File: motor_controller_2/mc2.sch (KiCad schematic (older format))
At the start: 56 parts, among them P1 Battery, P2 Servo, P3 Uart, P4 Ultrasound, P5 Motor left, P6 Motor right, P7 ISP, U1 TS1117E33, U2 TS1117E50, U3 PC817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

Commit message: footprints assigned (not ready)
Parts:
- added P8: RPi 5V, Pin_Headers:Pin_Header_Straight_1x02, symbol CONN_01X02
- C10, C11, C12, C60, C61, C62, C63, C80, C81, C91: footprint (none) -> Capacitors_SMD:C_0603_HandSoldering
- C13, C14, C20, C21: footprint (none) -> SMD_Packages:SMD-1206_Pol
- C90: renamed from C91; footprint (none) -> Capacitors_SMD:C_0603_HandSoldering
- D10: footprint (none) -> Diodes_SMD:DO-214AB_Handsoldering
- D11, D60, D61, R11, R12, R13, R30, R31, R40, R41, R60, R61, R62, R70, R71, R72, R73, R74, R75, R76, R77: footprint (none) -> Resistors_SMD:R_0603_HandSoldering
- P1, P5, P6: footprint (none) -> Pin_Headers:Pin_Header_Straight_1x02
- P2, P3: footprint (none) -> Pin_Headers:Pin_Header_Straight_1x03
- P4: footprint (none) -> Pin_Headers:Pin_Header_Straight_1x04
- P7: footprint (none) -> Pin_Headers:Pin_Header_Straight_2x03
- R100: renamed from R70; footprint (none) -> Resistors_SMD:R_0603_HandSoldering
- R101: renamed from R71; footprint (none) -> Resistors_SMD:R_0603_HandSoldering
- U3, U4: footprint DIP-4 -> (none)
- U6: footprint TQFP44 -> Housings_QFP:TQFP-44_10x10mm_Pitch0.8mm
- renumbered U7 to U10
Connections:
- net +5VD: now also P8.2 (P2)
- net GND: now also P8.1 (P1)

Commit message: footprint assignments (not ready)
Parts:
- U1, U2: footprint (none) -> kicad-libraries:SOT-223
- U10: footprint (none) -> TO_SOT_Packages_SMD:SOT-23-5
- U5: footprint (none) -> Pin_Headers:Pin_Header_Angled_1x03
- U7: footprint (none) -> kicad-libraries:SOIC16
- U8, U9: footprint (none) -> kicad-libraries:SOP8
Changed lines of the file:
@@
 F 0 "U1" H 4500 600 50  0000 C CNN
 F 1 "TS1117E33" H 4400 1100 50  0000 C CNN
-F 2 "" H 4400 850 50  0001 C CNN
+F 2 "kicad-libraries:SOT-223" H 4400 850 50  0001 C CNN
 F 3 "" H 4400 850 50  0000 C CNN
 	1    4400 850
@@
 F 0 "U2" H 4500 1950 50  0000 C CNN
 F 1 "TS1117E50" H 4400 2450 50  0000 C CNN
-F 2 "" H 4400 2200 50  0001 C CNN
+F 2 "kicad-libraries:SOT-223" H 4400 2200 50  0001 C CNN
 F 3 "" H 4400 2200 50  0000 C CNN
 	1    4400 2200
@@
 F 0 "U5" H 6750 704 50  0000 C CNN
 F 1 "R-78Bxx" H 6600 1100 50  0000 C CNN
-F 2 "" H 6600 900 50  0001 C CNN
+F 2 "Pin_Headers:Pin_Header_Angled_1x03" H 6600 900 50  0001 C CNN
 F 3 "" H 6600 900 50  0000 C CNN
 	1    6600 900
@@
 F 0 "U10" H 7800 4400 60  0000 C CNN
 F 1 "ts321" H 7850 3950 60  0000 C CNN
-F 2 "" H 7550 4450 60  0001 C CNN
+F 2 "TO_SOT_Packages_SMD:SOT-23-5" H 7550 4450 60  0001 C CNN
 F 3 "" H 7550 4450 60  0000 C CNN
 	1    7450 4200
@@
 F 0 "U8" H 9450 5150 60  0000 C CNN
 F 1 "BD6221F-E2" H 9650 4550 60  0000 C CNN
-F 2 "" H 10000 4700 60  0001 C CNN
+F 2 "kicad-libraries:SOP8" H 10000 4700 60  0001 C CNN
 F 3 "" H 10000 4700 60  0000 C CNN
 	1    9650 4850
@@
 F 0 "U7" H 1700 6200 50  0000 L CNN
 F 1 "TLP280" H 1700 5800 50  0000 L CNN
-F 2 "" H 1700 5800 50  0001 L CIN
+F 2 "kicad-libraries:SOIC16" H 1700 5800 50  0001 L CIN
 F 3 "" H 1900 6000 50  0000 L CNN
 	1    1900 6000
@@
 F 0 "U7" H 1700 7400 50  0000 L CNN
 F 1 "TLP280" H 1700 7000 50  0000 L CNN
-F 2 "" H 1700 7000 50  0001 L CIN
+F 2 "kicad-libraries:SOIC16" H 1700 7000 50  0001 L CIN
 F 3 "" H 1900 7200 50  0000 L CNN
 	2    1900 7200
@@
 F 0 "U7" H 4450 6200 50  0000 L CNN
 F 1 "TLP280" H 4450 5800 50  0000 L CNN
-F 2 "" H 4450 5800 50  0001 L CIN
+F 2 "kicad-libraries:SOIC16" H 4450 5800 50  0001 L CIN
 F 3 "" H 4650 6000 50  0000 L CNN
 	3    4650 6000
@@
 F 0 "U7" H 4450 7400 50  0000 L CNN
 F 1 "TLP280" H 4450 7000 50  0000 L CNN
-F 2 "" H 4450 7000 50  0001 L CIN
+F 2 "kicad-libraries:SOIC16" H 4450 7000 50  0001 L CIN
 F 3 "" H 4650 7200 50  0000 L CNN
 	4    4650 7200
@@
 F 0 "U9" H 9450 6050 60  0000 C CNN
 F 1 "BD6221F-E2" H 9650 5450 60  0000 C CNN
-F 2 "" H 10000 5600 60  0001 C CNN
+F 2 "kicad-libraries:SOP8" H 10000 5600 60  0001 C CNN
 F 3 "" H 10000 5600 60  0000 C CNN
 	1    9650 5750

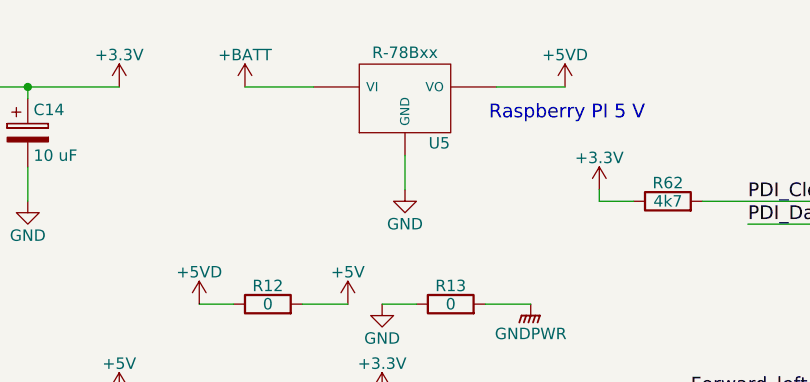
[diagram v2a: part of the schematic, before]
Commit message: all footprints assigned
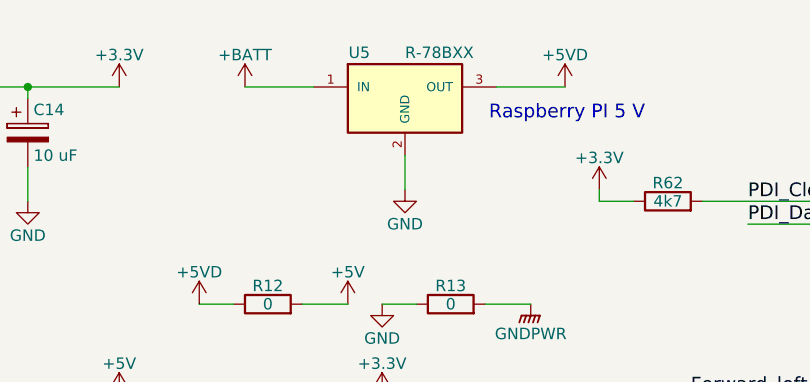
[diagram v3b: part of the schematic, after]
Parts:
- removed U5: R-78Bxx, Pin_Headers:Pin_Header_Angled_1x03, symbol 7805
- added U5: R-78BXX, TO_SOT_Packages_THT:TO-220_Neutral123_Vertical, symbol LM7806CT
- U3, U4: footprint (none) -> rzfp:OPB606
- U8, U9: footprint kicad-libraries:SOP8 -> Housings_SOIC:SOIC-8_3.9x4.9mm_Pitch1.27mm
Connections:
- net +5VD: now also U5.3 (OUT)
- net +BATT: now also U5.1 (IN)
- net GND: now also U5.2 (GND)
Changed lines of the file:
@@
 F 0 "U3" H 4100 3900 50  0000 L CNN
 F 1 "PC817" H 4300 3900 50  0000 L CNN
-F 2 "" H 4100 3500 50  0001 L CIN
+F 2 "rzfp:OPB606" H 4100 3500 50  0001 L CIN
 F 3 "" H 4300 3700 50  0000 L CNN
 	1    4300 3700
@@
 F 0 "U4" H 4100 5200 50  0000 L CNN
 F 1 "PC817" H 4300 5200 50  0000 L CNN
-F 2 "" H 4100 4800 50  0001 L CIN
+F 2 "rzfp:OPB606" H 4100 4800 50  0001 L CIN
 F 3 "" H 4300 5000 50  0000 L CNN
 	1    4300 5000
@@
 Text Label 5300 4900 2    60   ~ 0
 Rpm_left
-$Comp
-L 7805 U5
-U 1 1 57C32956
-P 6600 900
-F 0 "U5" H 6750 704 50  0000 C CNN
-F 1 "R-78Bxx" H 6600 1100 50  0000 C CNN
-F 2 "Pin_Headers:Pin_Header_Angled_1x03" H 6600 900 50  0001 C CNN
-F 3 "" H 6600 900 50  0000 C CNN
-	1    6600 900
-	1    0    0    -1
-$EndComp
 $Comp
 L +BATT #PWR026
@@
 F 0 "U8" H 9450 5150 60  0000 C CNN
 F 1 "BD6221F-E2" H 9650 4550 60  0000 C CNN
-F 2 "kicad-libraries:SOP8" H 10000 4700 60  0001 C CNN
+F 2 "Housings_SOIC:SOIC-8_3.9x4.9mm_Pitch1.27mm" H 10000 4700 60  0001 C CNN
 F 3 "" H 10000 4700 60  0000 C CNN
 	1    9650 4850
@@
 F 0 "U9" H 9450 6050 60  0000 C CNN
 F 1 "BD6221F-E2" H 9650 5450 60  0000 C CNN
-F 2 "kicad-libraries:SOP8" H 10000 5600 60  0001 C CNN
+F 2 "Housings_SOIC:SOIC-8_3.9x4.9mm_Pitch1.27mm" H 10000 5600 60  0001 C CNN
 F 3 "" H 10000 5600 60  0000 C CNN
 	1    9650 5750
@@
 	-1   0    0    1
 $EndComp
+$Comp
+L LM7806CT U5
+U 1 1 57CAF2D1
+P 6600 900
+F 0 "U5" H 6400 1100 50  0000 C CNN
+F 1 "R-78BXX" H 6600 1100 50  0000 L CNN
+F 2 "TO_SOT_Packages_THT:TO-220_Neutral123_Vertical" H 6600 1000 50  0001 C CIN
+F 3 "" H 6600 900 50  0000 C CNN
+	1    6600 900
+	1    0    0    -1
+$EndComp
 $EndSCHEMATC

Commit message: footprints finalized
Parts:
- D10: footprint Diodes_SMD:DO-214AB_Handsoldering -> Diodes_SMD:DO-214BA
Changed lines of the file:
@@
 F 0 "D10" H 1500 950 50  0000 C CNN
 F 1 "SS24" H 1500 750 50  0000 C CNN
-F 2 "Diodes_SMD:DO-214AB_Handsoldering" H 1500 850 50  0001 C CNN
+F 2 "Diodes_SMD:DO-214BA" H 1500 850 50  0001 C CNN
 F 3 "" H 1500 850 50  0000 C CNN
 	1    1500 850

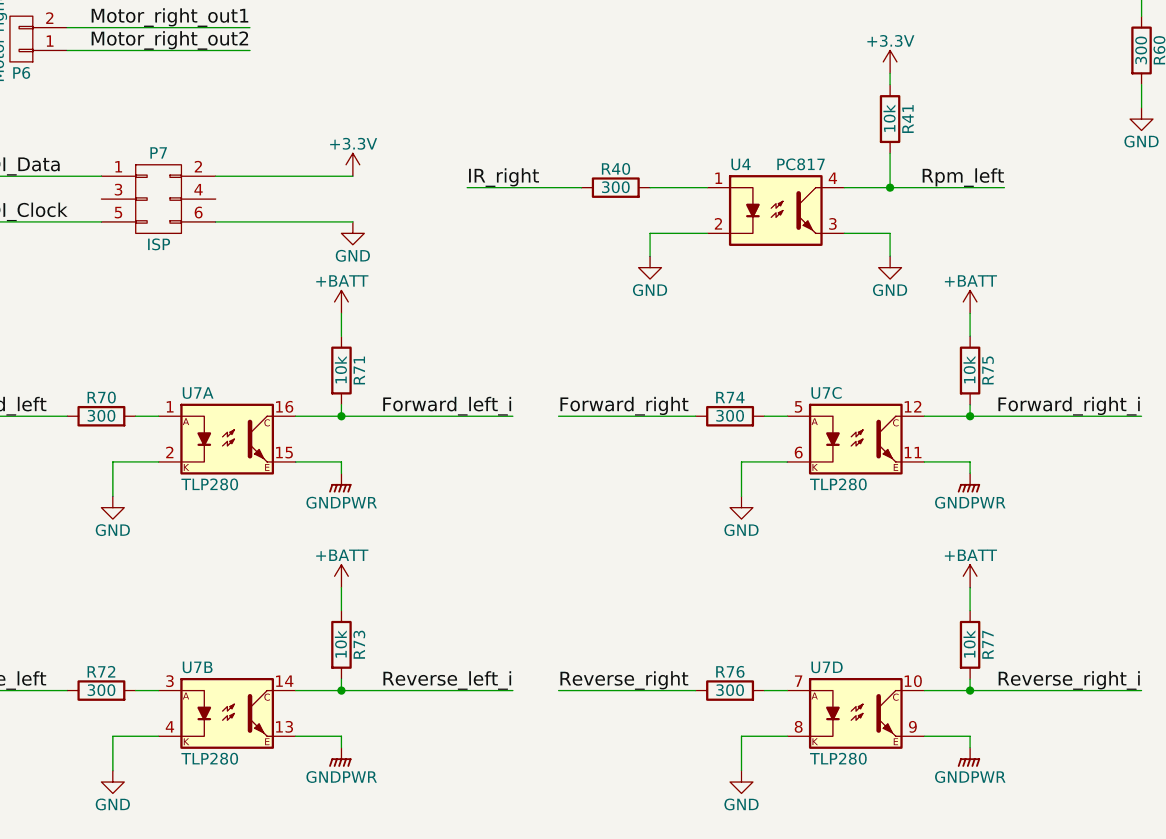
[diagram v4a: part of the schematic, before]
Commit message: component layout of motor controller
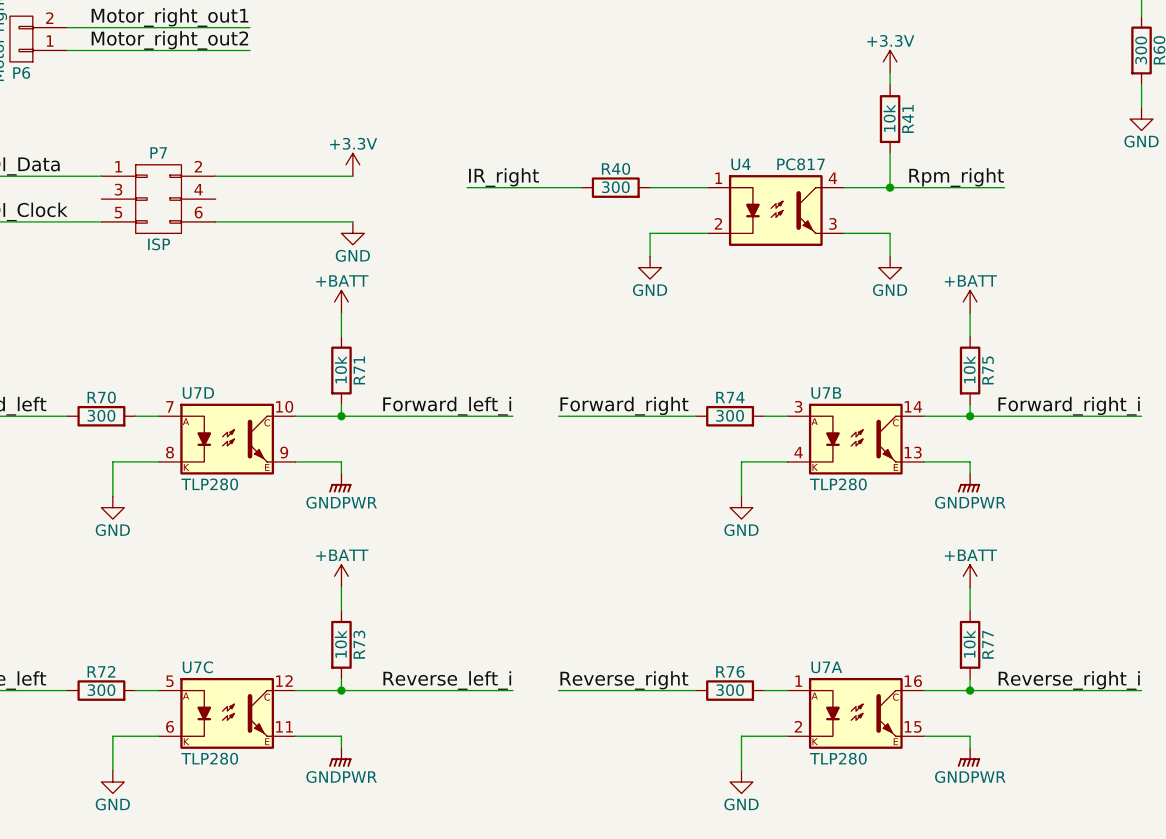
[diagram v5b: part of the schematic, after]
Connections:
- net Forward_left_i: now also U7.10; no longer U7.16
- net Forward_right_i: now also U7.14; no longer U7.12
- net GND: now also U7.2, U7.4, U7.6, U7.8; no longer U7.2, U7.4, U7.6, U7.8
- net GNDPWR: now also U7.11, U7.13, U7.15, U7.9; no longer U7.11, U7.13, U7.15, U7.9
- net Reverse_left_i: now also U7.12; no longer U7.14
- net Reverse_right_i: now also U7.16; no longer U7.10
- net Rpm_left: no longer R41.2, U4.4
- net Rpm_right: now also R41.2, U4.4
- net at R70.2: now also U7.7; no longer U7.1
- net at R72.2: now also U7.5; no longer U7.3
- net at R74.2: now also U7.3; no longer U7.5
- net at R76.2: now also U7.1; no longer U7.7
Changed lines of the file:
@@
 $EndComp
 Text Label 5300 4900 2    60   ~ 0
-Rpm_left
+Rpm_right
 $Comp
 L +BATT #PWR026
@@
 $Comp
 L OPTO-TRANSISTOR-4 U7
-U 1 1 57C45CF6
+U 4 1 57C45CF6
 P 1900 6000
 F 0 "U7" H 1700 6200 50  0000 L CNN
@@
 F 2 "kicad-libraries:SOIC16" H 1700 5800 50  0001 L CIN
 F 3 "" H 1900 6000 50  0000 L CNN
-	1    1900 6000
+	4    1900 6000
 	1    0    0    -1
 $EndComp
@@
 $Comp
 L OPTO-TRANSISTOR-4 U7
-U 2 1 57C4A74F
+U 3 1 57C4A74F
 P 1900 7200
 F 0 "U7" H 1700 7400 50  0000 L CNN
@@
 F 2 "kicad-libraries:SOIC16" H 1700 7000 50  0001 L CIN
 F 3 "" H 1900 7200 50  0000 L CNN
-	2    1900 7200
+	3    1900 7200
 	1    0    0    -1
 $EndComp
@@
 $Comp
 L OPTO-TRANSISTOR-4 U7
-U 3 1 57C4C48A
+U 2 1 57C4C48A
 P 4650 6000
 F 0 "U7" H 4450 6200 50  0000 L CNN
@@
 F 2 "kicad-libraries:SOIC16" H 4450 5800 50  0001 L CIN
 F 3 "" H 4650 6000 50  0000 L CNN
-	3    4650 6000
+	2    4650 6000
 	1    0    0    -1
 $EndComp
@@
 $Comp
 L OPTO-TRANSISTOR-4 U7
-U 4 1 57C4C4AF
+U 1 1 57C4C4AF
 P 4650 7200
 F 0 "U7" H 4450 7400 50  0000 L CNN
@@
 F 2 "kicad-libraries:SOIC16" H 4450 7000 50  0001 L CIN
 F 3 "" H 4650 7200 50  0000 L CNN
-	4    4650 7200
-	1    0    0    -1
-$EndComp
+	1    4650 7200
+	1    0    0    -1
+$EndComp

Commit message: pcb design finalized
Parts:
- removed P4: Ultrasound, Pin_Headers:Pin_Header_Straight_1x04, symbol CONN_01X04
- added P4: Ultrasound, Pin_Headers:Pin_Header_Straight_1x06, symbol CONN_01X06
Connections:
- net +5V: now also P4.5 (P5)
- net +BATT: now also P4.6 (P6)
- net GND: now also P4.1 (P1)
- net Pulse_in: now also P4.3 (P3)
- net Pulse_out: now also P4.4 (P4)
- net ADC: now reaches U6.40 (AREFA/AC0/ADC0/PA0)
- net ADC: now also P4.2 (P2)
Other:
- note removed: "PCB:\n - isp tavolabb a mikrokontrollertol\n - headereknek nagyobb furat\n - headerre konnektornak utananezni\n - panelmeret 12x5.5 cm\n"
- moved on the sheet: P5, P6
